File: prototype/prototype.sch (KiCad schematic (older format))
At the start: 8 parts, among them P1 CONN_25X2, P2 CONN_25X2, U1 MC68SEC000

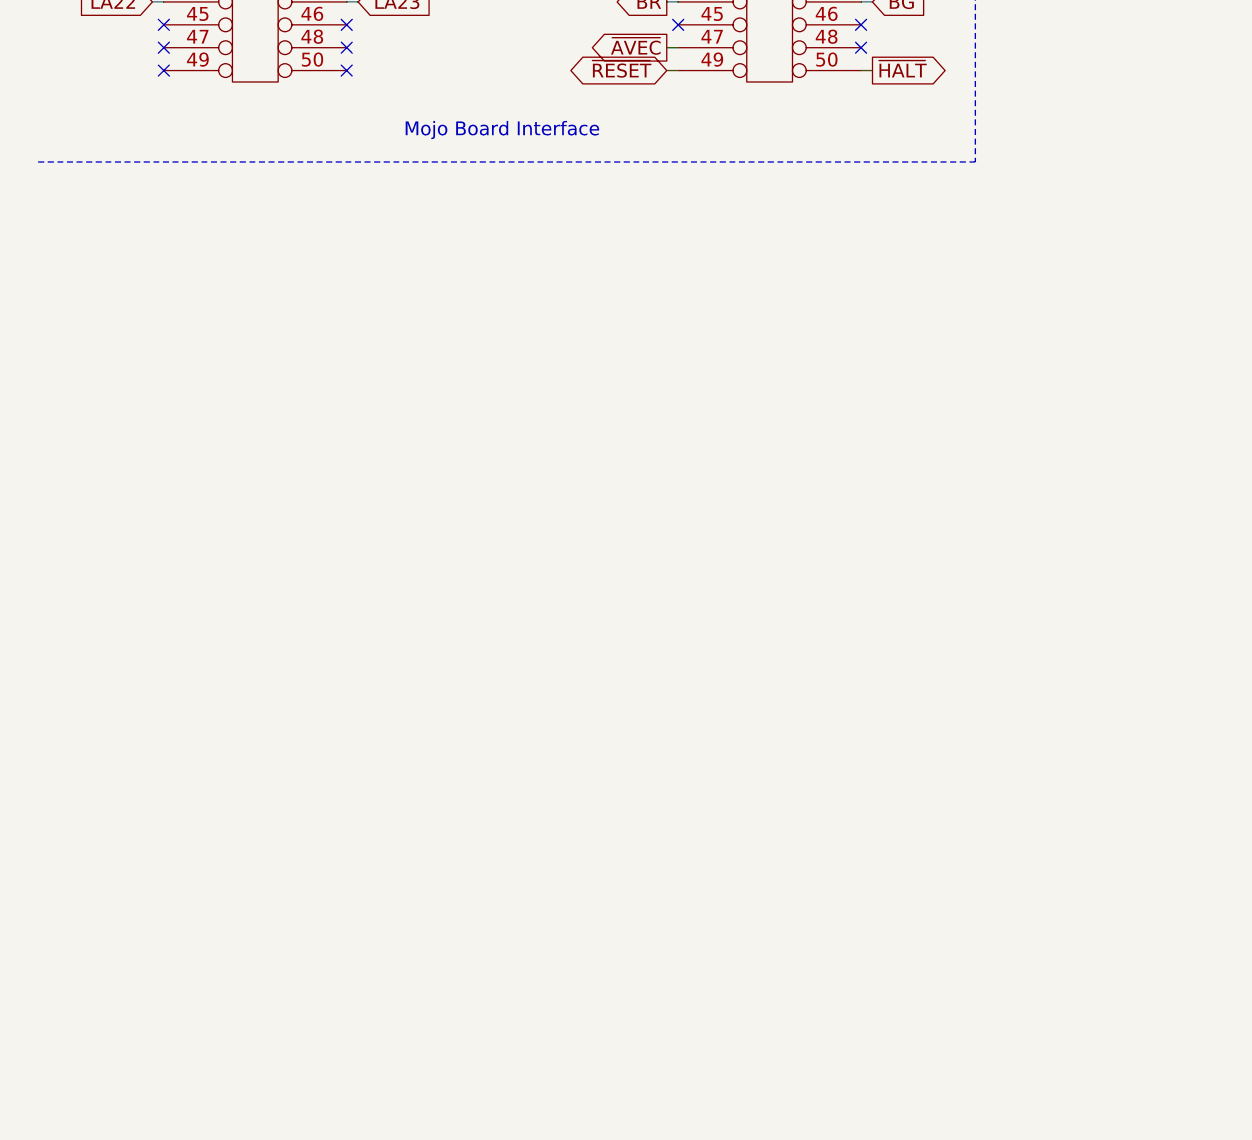
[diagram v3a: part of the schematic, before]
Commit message: VGA output stage for prototype PCB.
A simple resistor-based DAC is used to create the analog color signals.
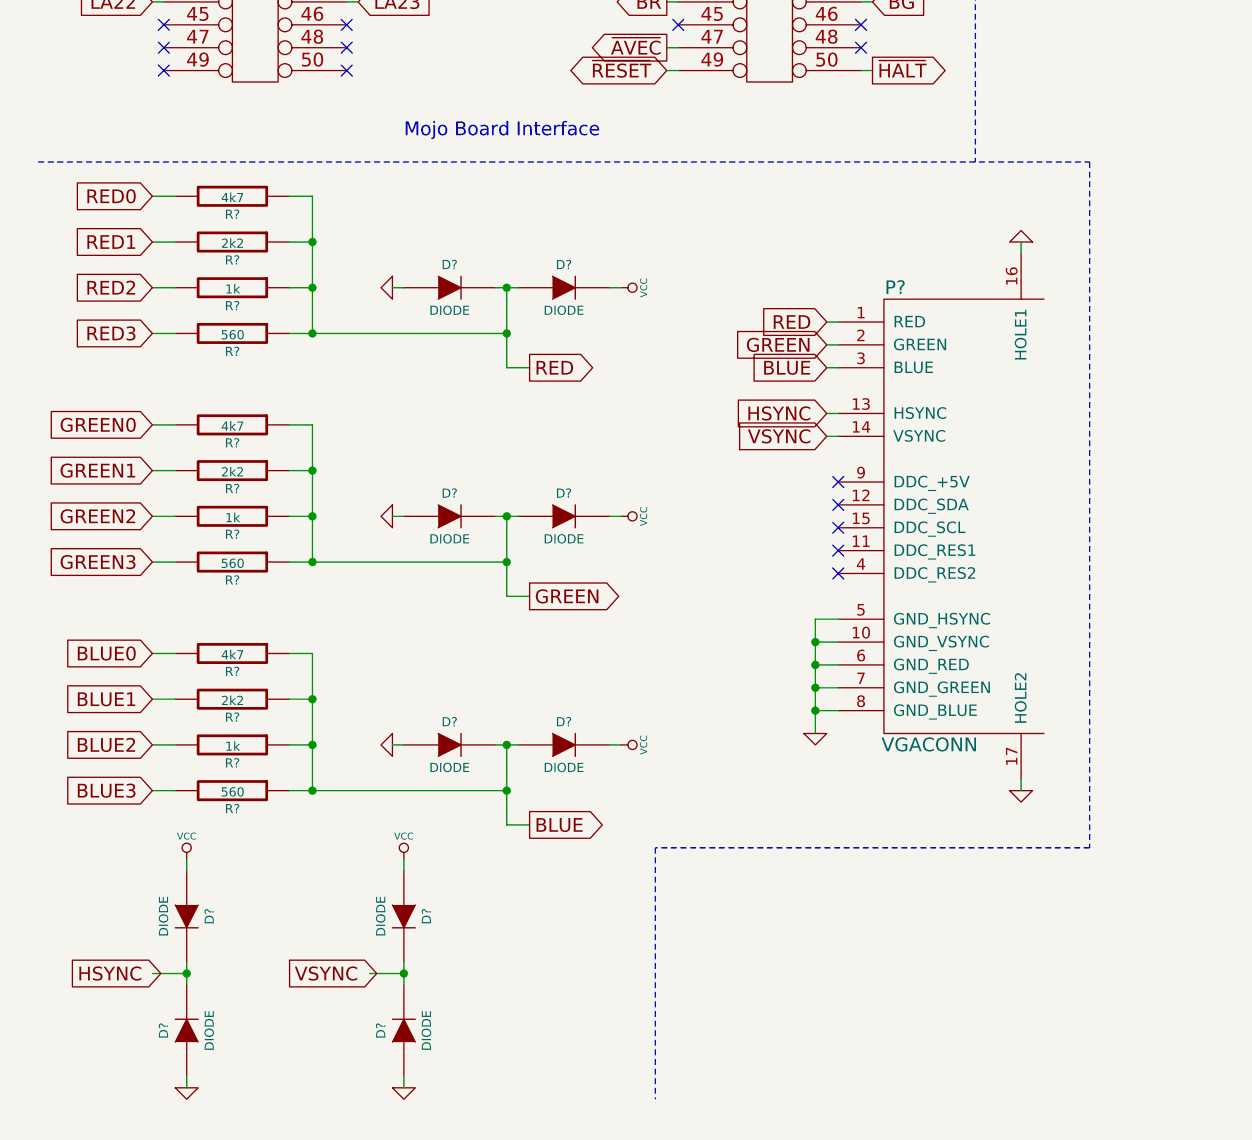
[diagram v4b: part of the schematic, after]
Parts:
- added D? (x10): DIODE, symbol DIODE
- added P?: VGACONN, symbol VGACONN
- added R? (x3): 4k7, symbol R
- added R? (x3): 2k2, symbol R
- added R? (x3): 1k, symbol R
- added R? (x3): 560, symbol R
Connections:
- net BLUE0: now also R?.2
- net BLUE1: now also R?.2
- net BLUE2: now also R?.2
- net BLUE3: now also R?.2
- net GND: now also D?.1 (A), D?.1 (A), D?.1 (A), D?.1 (A), D?.1 (A), P?.10 (GND_VSYNC), P?.16 (HOLE1), P?.17 (HOLE2), P?.5 (GND_HSYNC), P?.6 (GND_RED), P?.7 (GND_GREEN), P?.8 (GND_BLUE)
- net GREEN0: now also R?.2
- net GREEN1: now also R?.2
- net GREEN2: now also R?.2
- net GREEN3: now also R?.2
- net HSYNC: now also P?.13 (HSYNC)
- net RED0: now also R?.2
- net RED1: now also R?.2
- net RED2: now also R?.2
- net RED3: now also R?.2
- net VCC: now also D?.1 (A), D?.1 (A), D?.2 (K), D?.2 (K), D?.2 (K)
- net VSYNC: now also P?.14 (VSYNC)
- new net: D?.2 (K), D?.2 (K) (x2)
- new net BLUE: D?.1 (A), D?.2 (K), P?.3 (BLUE), R?.1, R?.1, R?.1, R?.1
- new net GREEN: D?.1 (A), D?.2 (K), P?.2 (GREEN), R?.1, R?.1, R?.1, R?.1
- new net RED: D?.1 (A), D?.2 (K), P?.1 (RED), R?.1, R?.1, R?.1, R?.1
- no-connect marks 14 -> 19

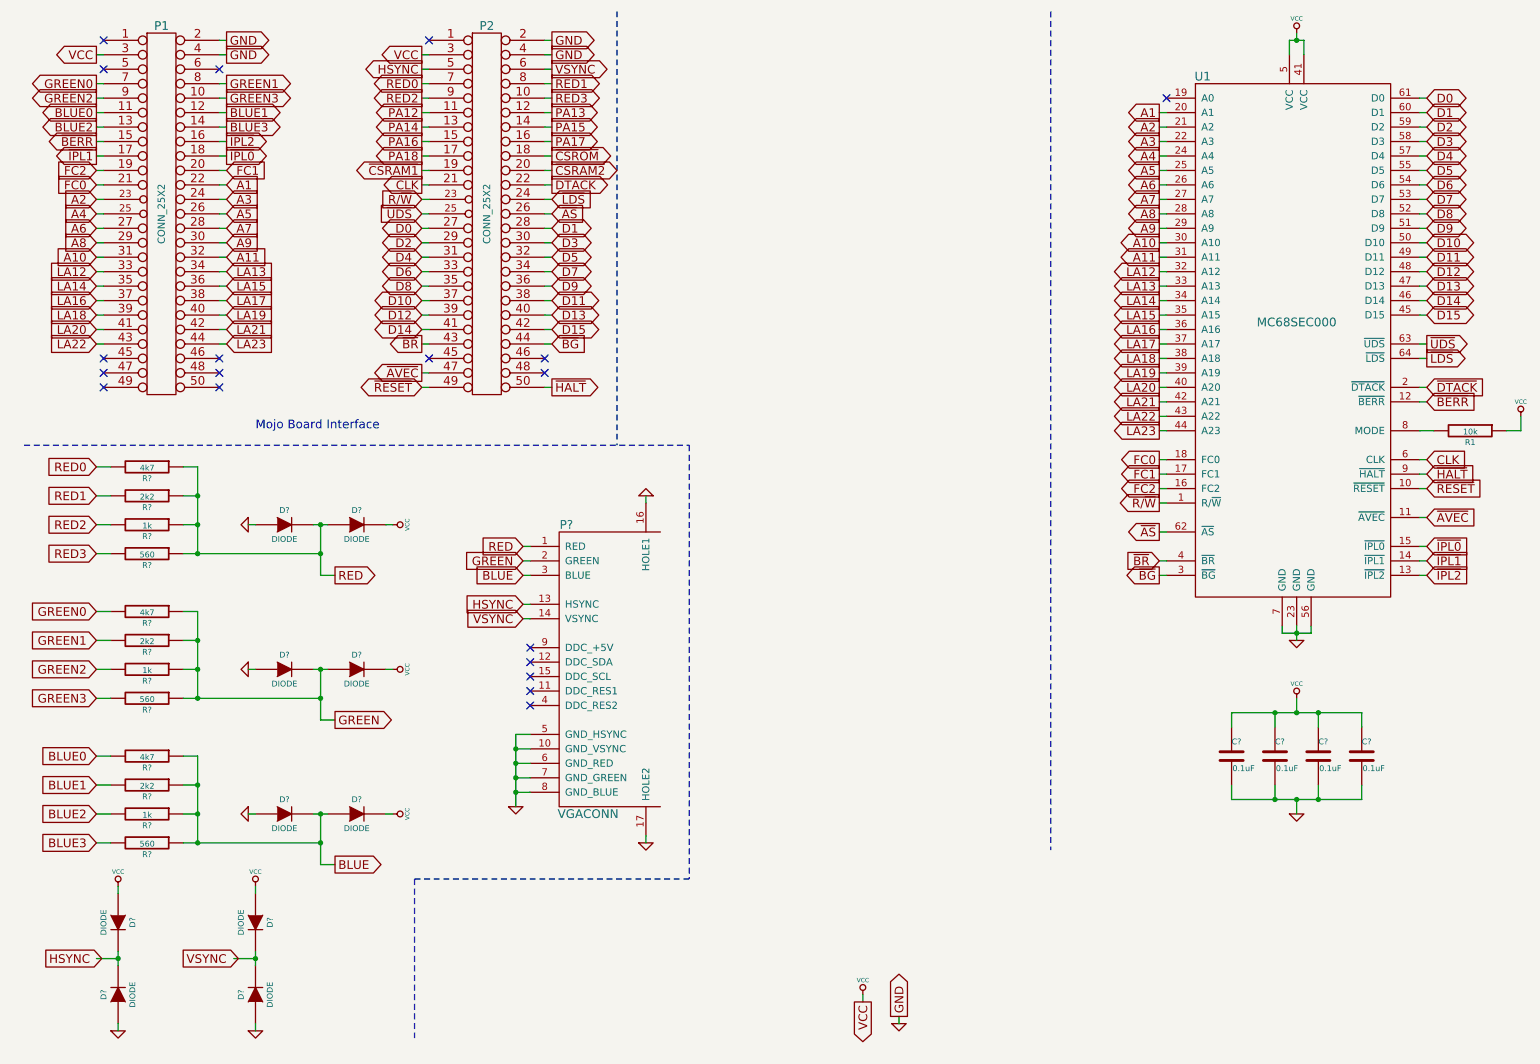
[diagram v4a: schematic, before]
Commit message: Annotate the schematic components.
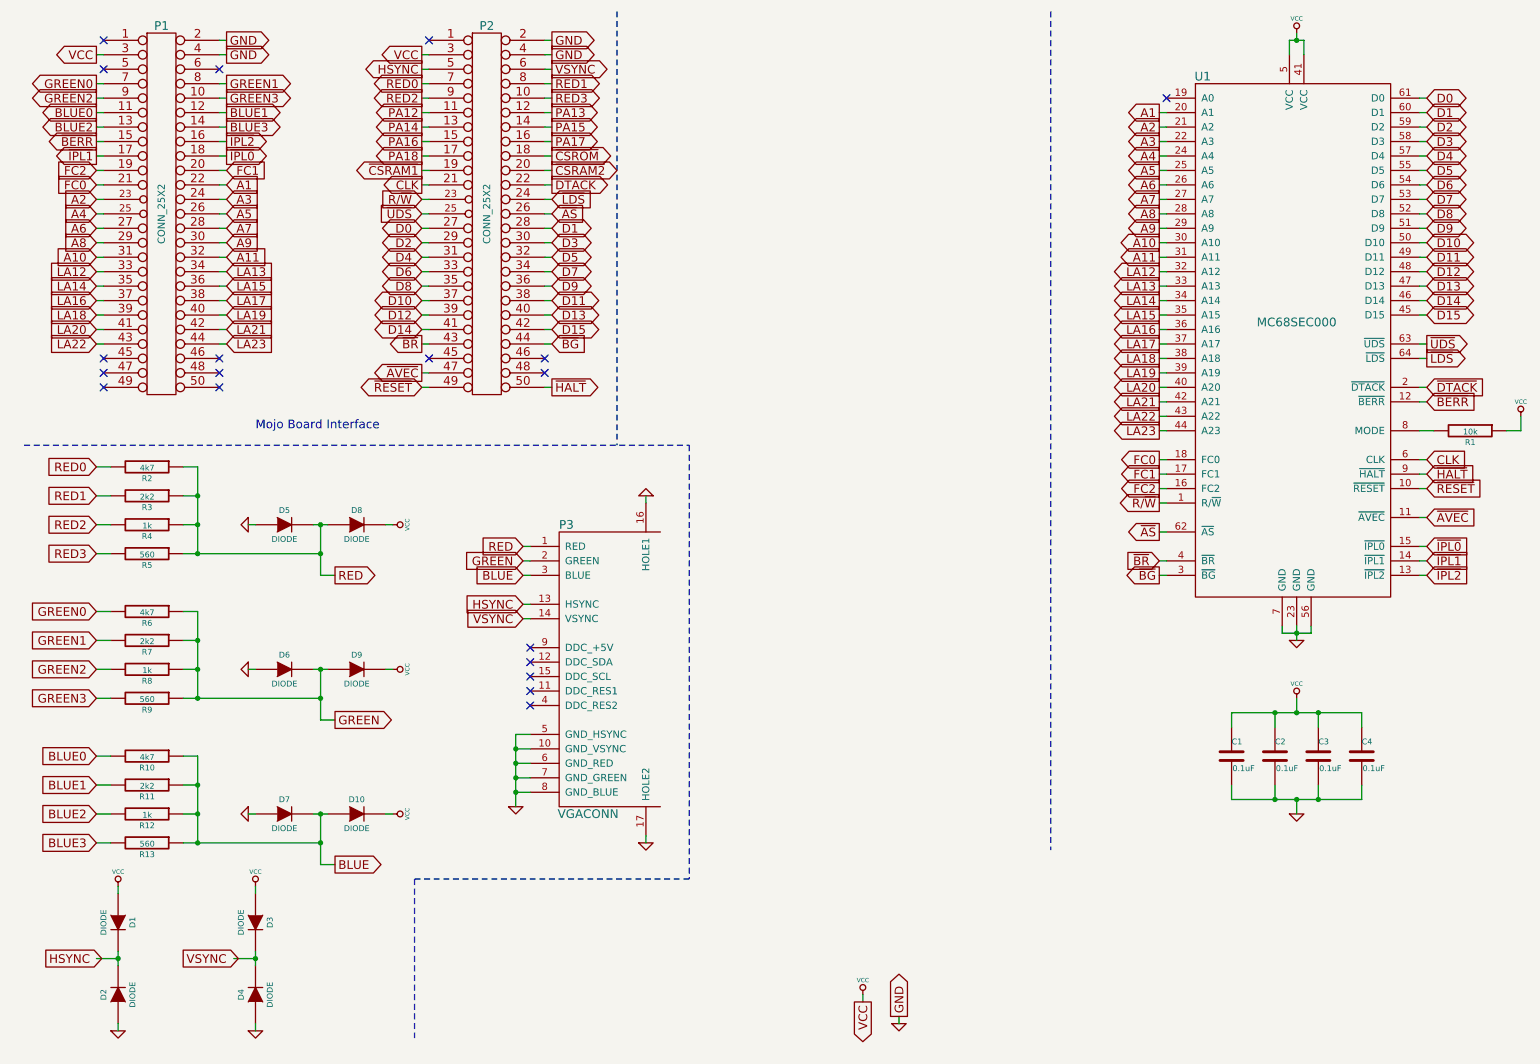
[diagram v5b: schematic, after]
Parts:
- gave numbers to parts that had none: 27
